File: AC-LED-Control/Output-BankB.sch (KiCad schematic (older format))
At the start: 40 parts, among them P201 CONN_01X02, P202 CONN_01X02, P203 CONN_01X02, P204 CONN_01X02, P205 CONN_01X02, P206 CONN_01X02, P207 CONN_01X02, P208 CONN_01X02, U201 TRIAC, U202 TRIAC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

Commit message: Finished final associations and tweaks
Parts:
- removed P201, P202, P203, P204, P205, P206, P207, P208: CONN_01X02, Pin_Headers:Pin_Header_Straight_1x02_Pitch2.54mm, symbol CONN_01X02
- added J301, J302, J303, J304, J305, J306, J307, J308: Conn_01x02, Connectors_OnShore:OSTTC022162, symbol Conn_01x02
- U201, U202, U203, U204, U205, U206, U207, U208: footprint (none) -> Power-Packages:DPAK
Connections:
- net AC-H: now also J301.2 (Pin_2), J302.2 (Pin_2), J303.2 (Pin_2), J304.2 (Pin_2), J305.2 (Pin_2), J306.2 (Pin_2), J307.2 (Pin_2), J308.2 (Pin_2)
- net AC_LOAD-A: now also J301.1 (Pin_1)
- net AC_LOAD-B: now also J303.1 (Pin_1)
- net AC_LOAD-C: now also J305.1 (Pin_1)
- net AC_LOAD-D: now also J307.1 (Pin_1)
- net AC_LOAD-E: now also J302.1 (Pin_1)
- net AC_LOAD-F: now also J304.1 (Pin_1)
- net AC_LOAD-G: now also J306.1 (Pin_1)
- net AC_LOAD-H: now also J308.1 (Pin_1)

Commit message: Changed TRIAC from DPAK part to T0-202-3 part.
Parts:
- U201, U202, U203, U204, U205, U206, U207, U208: footprint Power-Packages:DPAK -> Power-Packages:TO-202-3-Vertical
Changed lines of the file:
@@
 F 0 "U301" H 4050 1800 50  0000 C CNN
 F 1 "TRIAC" H 4000 1200 50  0000 C CNN
-F 2 "Power-Packages:DPAK" H 4300 1450 50  0001 C CNN
+F 2 "Power-Packages:TO-202-3-Vertical" H 4300 1450 50  0001 C CNN
 F 3 "" H 4300 1450 50  0000 C CNN
 	1    4300 1450
@@
 F 0 "U303" H 4050 2750 50  0000 C CNN
 F 1 "TRIAC" H 4000 2150 50  0000 C CNN
-F 2 "Power-Packages:DPAK" H 4300 2400 50  0001 C CNN
+F 2 "Power-Packages:TO-202-3-Vertical" H 4300 2400 50  0001 C CNN
 F 3 "" H 4300 2400 50  0000 C CNN
 	1    4300 2400
@@
 F 0 "U305" H 4050 3700 50  0000 C CNN
 F 1 "TRIAC" H 4000 3100 50  0000 C CNN
-F 2 "Power-Packages:DPAK" H 4300 3350 50  0001 C CNN
+F 2 "Power-Packages:TO-202-3-Vertical" H 4300 3350 50  0001 C CNN
 F 3 "" H 4300 3350 50  0000 C CNN
 	1    4300 3350
@@
 F 0 "U307" H 4050 4650 50  0000 C CNN
 F 1 "TRIAC" H 4000 4050 50  0000 C CNN
-F 2 "Power-Packages:DPAK" H 4300 4300 50  0001 C CNN
+F 2 "Power-Packages:TO-202-3-Vertical" H 4300 4300 50  0001 C CNN
 F 3 "" H 4300 4300 50  0000 C CNN
 	1    4300 4300
@@
 F 0 "U302" H 8950 1800 50  0000 C CNN
 F 1 "TRIAC" H 8900 1200 50  0000 C CNN
-F 2 "Power-Packages:DPAK" H 9200 1450 50  0001 C CNN
+F 2 "Power-Packages:TO-202-3-Vertical" H 9200 1450 50  0001 C CNN
 F 3 "" H 9200 1450 50  0000 C CNN
 	1    9200 1450
@@
 F 0 "U304" H 8950 2750 50  0000 C CNN
 F 1 "TRIAC" H 8900 2150 50  0000 C CNN
-F 2 "Power-Packages:DPAK" H 9200 2400 50  0001 C CNN
+F 2 "Power-Packages:TO-202-3-Vertical" H 9200 2400 50  0001 C CNN
 F 3 "" H 9200 2400 50  0000 C CNN
 	1    9200 2400
@@
 F 0 "U306" H 8950 3700 50  0000 C CNN
 F 1 "TRIAC" H 8900 3100 50  0000 C CNN
-F 2 "Power-Packages:DPAK" H 9200 3350 50  0001 C CNN
+F 2 "Power-Packages:TO-202-3-Vertical" H 9200 3350 50  0001 C CNN
 F 3 "" H 9200 3350 50  0000 C CNN
 	1    9200 3350
@@
 F 0 "U308" H 8950 4650 50  0000 C CNN
 F 1 "TRIAC" H 8900 4050 50  0000 C CNN
-F 2 "Power-Packages:DPAK" H 9200 4300 50  0001 C CNN
+F 2 "Power-Packages:TO-202-3-Vertical" H 9200 4300 50  0001 C CNN
 F 3 "" H 9200 4300 50  0000 C CNN
 	1    9200 4300

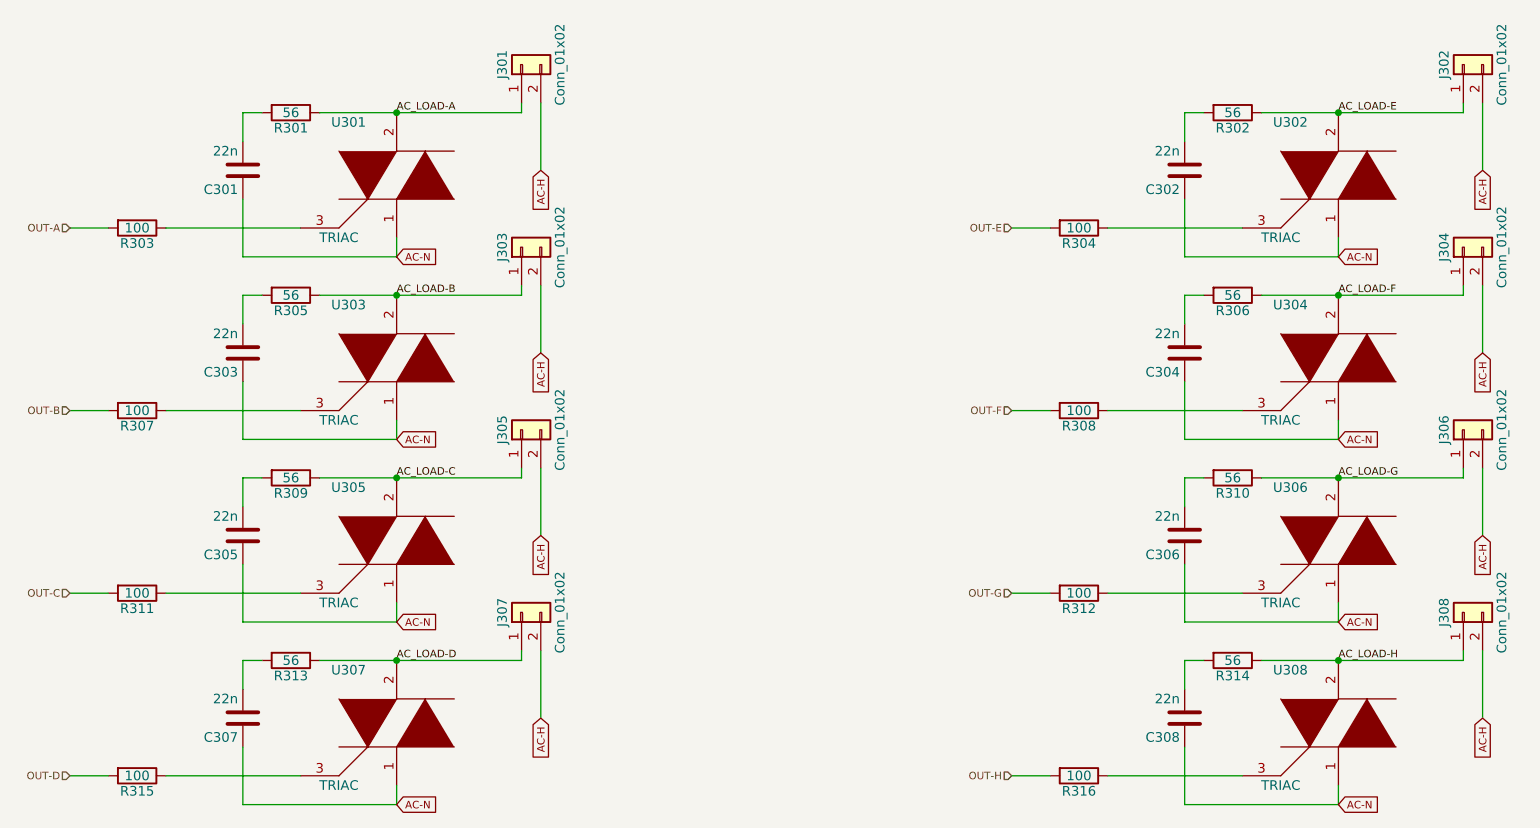
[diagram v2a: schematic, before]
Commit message: Lots of layout + added a diode.
I realised that the power regulator might need protection from the 3v3
line on the programming header.
Added a diode just in case.
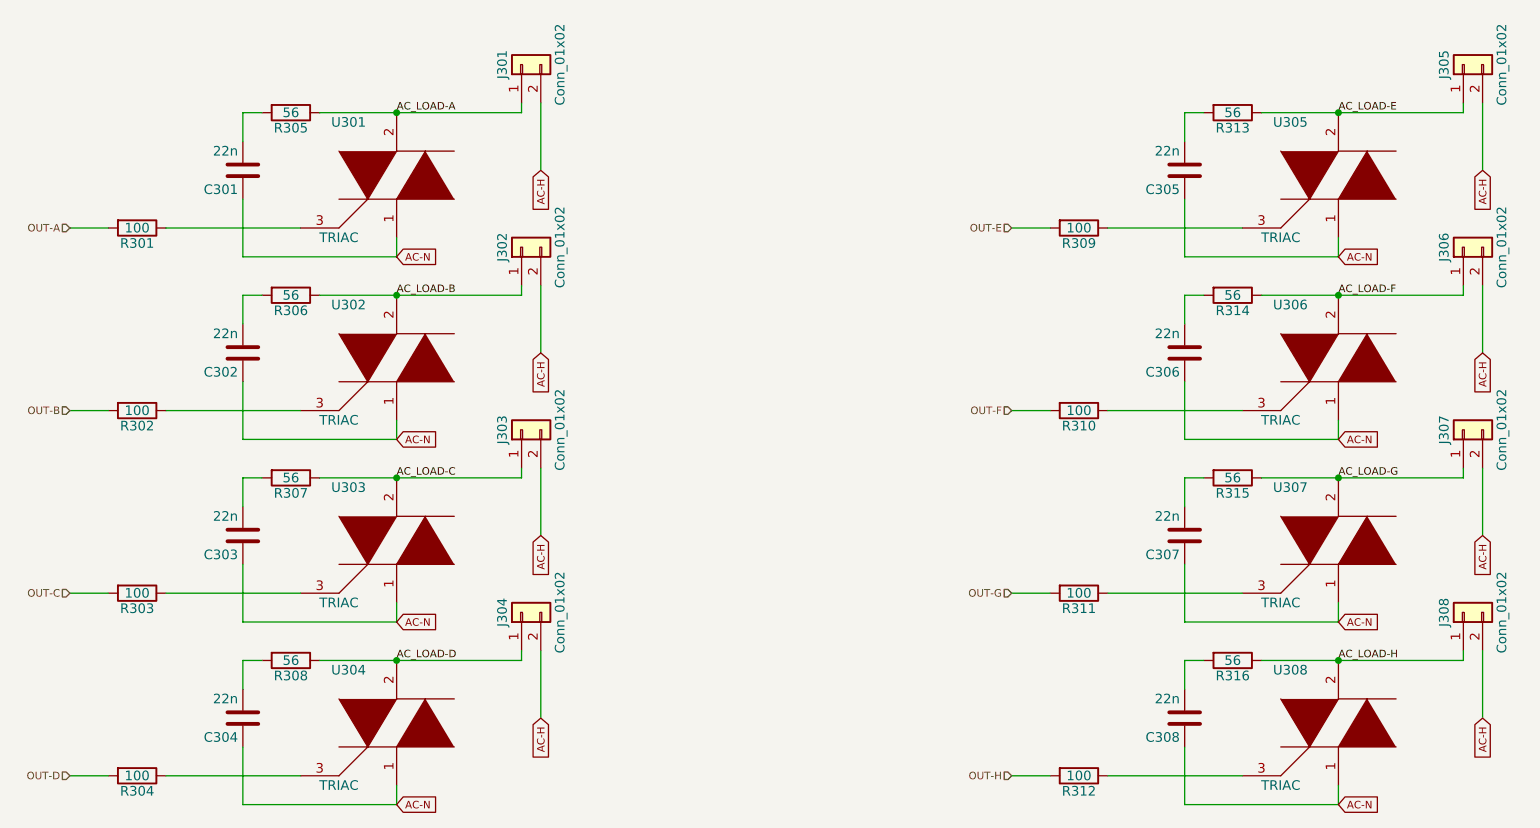
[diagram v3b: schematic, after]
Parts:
- renumbered J303 to J302, J305 to J303, J307 to J304, J302 to J305, J304 to J306, J306 to J307
